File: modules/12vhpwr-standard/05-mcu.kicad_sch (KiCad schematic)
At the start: 7 parts, among them SW1 BOOT, SW2 RESET, U1 ESP32-S3-MINI-1-N4R2

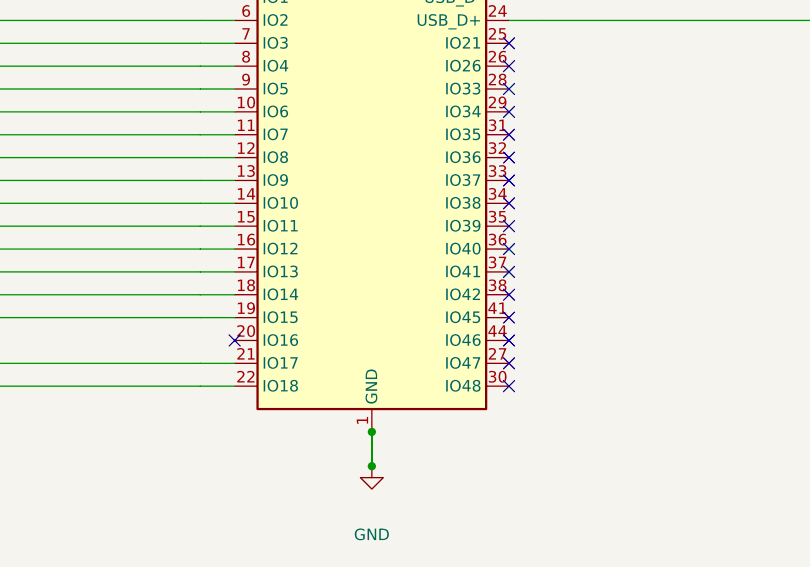
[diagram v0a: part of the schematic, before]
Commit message: All 5 sensing modules: add GPIO0 strapping-pin decoupler (match Hub)
Adds a 0.1uF cap (GPIO0->GND) + 10k pull-up (+3V3->GPIO0) to each module's
MCU sheet, matching the Hub (C8+R11). The modules already had BOOT+RESET
buttons and the EN reset RC; this closes the one systematic gap found in the
2026-07-07 decoupler audit -- the Espressif-recommended strapping-pin RC that
debounces the BOOT button and hardens GPIO0 against spurious download-mode
entry from noise. Owner directive 2026-07-07.

Parts: 24-pin C61/R61, eps/pcie-2/pcie-3 C41/R13, 12vhpwr C25/R24. Each lands
on /GPIO0 = {cap, pull-up, SW1(BOOT), MCU} with cap->GND and pull-up->+3V3,
netlist-verified 0 unexpected changes vs HEAD (an earlier placement that merged
GPIO0 with I2C_SCL/ISENSEP2 was caught by the diff and re-placed in
wire/label-clear space). ERC no_connect_connected=0 on all five.

Co-Authored-By: Claude Opus 4.8 <noreply@anthropic.com>
Claude-Session: https://claude.ai/code/session_01LvfqcnEeuin2oyJQw548EX
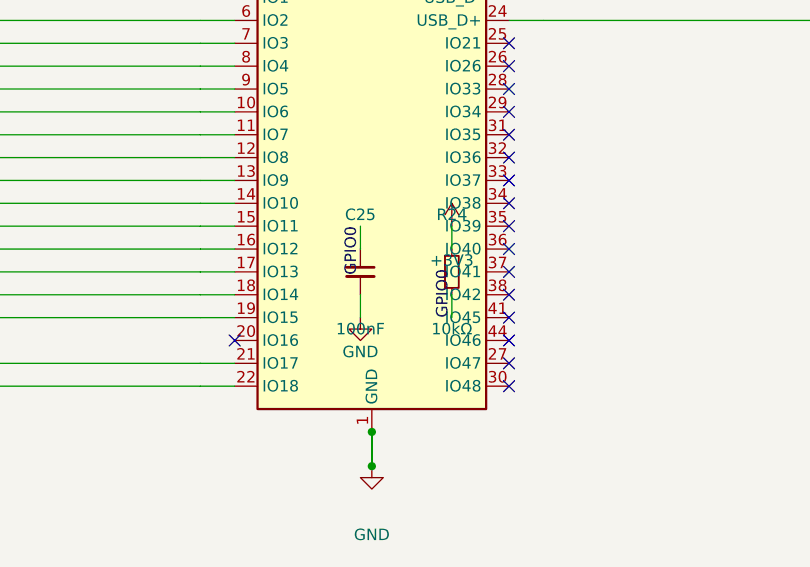
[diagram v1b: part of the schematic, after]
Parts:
- added C25: 100nF, cec-Capacitor_SMD:C_0402_1005Metric, symbol cec-vendor:C_Small
- added R24: 10kΩ, cec-Resistor_SMD:R_0402_1005Metric, symbol cec-vendor:R_Small
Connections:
- net +3V3: now also R24.1
- net GND: now also C25.2
- net GPIO0: now also C25.1, R24.2
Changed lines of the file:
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@@
 	(no_connect (at 257.81 123.19))
 	(no_connect (at 257.81 125.73))
+	(symbol
+		(lib_id "cec-vendor:C_Small")
+		(at 241.3 113.03 0)
+		(unit 1)
+		(exclude_from_sim no)
+		(in_bom yes)
+		(on_board yes)
+		(dnp no)
+		(fields_autoplaced yes)
+		(property "Reference" "C25" (at 241.3 106.68 0) (effects (font (size 1.27 1.27))))
+		(property "Value" "100nF" (at 241.3 119.38 0) (effects (font (size 1.27 1.27))))
+		(property "Footprint" "cec-Capacitor_SMD:C_0402_1005Metric" (at 241.3 113.03 0) (effects (font (size 1.27 1.27)) (hide yes)))
+		(property "Datasheet" "" (at 241.3 113.03 0) (effects (font (size 1.27 1.27)) (hide yes)))
+		(pin "1")
+		(pin "2")
+		(instances
+			(project "12vhpwr-standard-module"
+				(path "/436b24cb-7227-4a56-93c7-4c5d9a5d0058/5e9d5a2e-6b0a-4b6b-9a7a-2f7a7a8a1a05" (reference "C25") (unit 1))
+			)
+		)
+	)
+	(wire (pts (xy 241.3 110.49) (xy 241.3 107.95))
+		(stroke (width 0) (type default)))
+	(label "GPIO0" (at 241.3 107.95 90) (effects (font (size 1.27 1.27)) (justify right bottom)))
+	(wire (pts (xy 241.3 115.57) (xy 241.3 118.11))
+		(stroke (width 0) (type default)))
+	(symbol
+		(lib_id "cec-power:GND")
+		(at 241.3 118.11 0)
+		(unit 1)
+		(exclude_from_sim no)
+		(in_bom yes)
+		(on_board yes)
+		(dnp no)
+		(property "Reference" "#PWR01120" (at 241.3 115.57 0) (effects (font (size 1.27 1.27)) (hide yes)))
+		(property "Value" "GND" (at 241.3 121.92 0) (effects (font (size 1.27 1.27))))
+		(pin "1")
+		(instances
+			(project "12vhpwr-standard-module"
+				(path "/436b24cb-7227-4a56-93c7-4c5d9a5d0058/5e9d5a2e-6b0a-4b6b-9a7a-2f7a7a8a1a05" (reference "#PWR01120") (unit 1))
+			)
+		)
+	)
+	(symbol
+		(lib_id "cec-vendor:R_Small")
+		(at 251.46 113.03 0)
+		(unit 1)
+		(exclude_from_sim no)
+		(in_bom yes)
+		(on_board yes)
+		(dnp no)
+		(fields_autoplaced yes)
+		(property "Reference" "R24" (at 251.46 106.68 0) (effects (font (size 1.27 1.27))))
+		(property "Value" "10kΩ" (at 251.46 119.38 0) (effects (font (size 1.27 1.27))))
+		(property "Footprint" "cec-Resistor_SMD:R_0402_1005Metric" (at 251.46 113.03 0) (effects (font (size 1.27 1.27)) (hide yes)))
+		(property "Datasheet" "" (at 251.46 113.03 0) (effects (font (size 1.27 1.27)) (hide yes)))
+		(pin "1")
+		(pin "2")
+		(instances
+			(project "12vhpwr-standard-module"
+				(path "/436b24cb-7227-4a56-93c7-4c5d9a5d0058/5e9d5a2e-6b0a-4b6b-9a7a-2f7a7a8a1a05" (reference "R24") (unit 1))
+			)
+		)
+	)
+	(wire (pts (xy 251.46 110.49) (xy 251.46 107.95))
+		(stroke (width 0) (type default)))
+	(symbol
+		(lib_id "cec-power:+3V3")
+		(at 251.46 107.95 0)
+		(unit 1)
+		(exclude_from_sim no)
+		(in_bom yes)
+		(on_board yes)
+		(dnp no)
+		(property "Reference" "#PWR01121" (at 251.46 105.41 0) (effects (font (size 1.27 1.27)) (hide yes)))
+		(property "Value" "+3V3" (at 251.46 111.76 0) (effects (font (size 1.27 1.27))))
+		(pin "1")
+		(instances
+			(project "12vhpwr-standard-module"
+				(path "/436b24cb-7227-4a56-93c7-4c5d9a5d0058/5e9d5a2e-6b0a-4b6b-9a7a-2f7a7a8a1a05" (reference "#PWR01121") (unit 1))
+			)
+		)
+	)
+	(wire (pts (xy 251.46 115.57) (xy 251.46 118.11))
+		(stroke (width 0) (type default)))
+	(label "GPIO0" (at 251.46 118.11 270) (effects (font (size 1.27 1.27)) (justify left bottom)))
 	(sheet_instances
 		(path "/5e9d5a2e-6b0a-4b6b-9a7a-2f7a7a8a1a05"

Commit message: 12vhpwr-standard: J2 fan port grows to 3-pin firmware-switched leg
Owner-ratified fan-control leg (3-pin tach, default-on): J2 becomes a
3-pin JST PH B3B-PH-K-S (new cec:CEC_FAN_3P symbol, LCSC C131339, DNP
posture preserved from the prior 2-pin provision). Q1 = AO3400A
low-side NMOS (new reusable cec-vendor:Q_NMOS_GSD symbol) switches the
fan return to GND, default-on via a 10k gate pullup to +3V3 with a
100R series R from a free ESP32-S3 GPIO (IO21); D5 = SS34 flyback
diode across the fan; the open-collector TACH line gets a 10k pullup
plus a 1k series R into a second free GPIO (IO47). Both GPIOs were
picked from the real ERC no_connect list, avoiding the ESP32-S3-MINI-1
N4R2's octal-PSRAM-reserved GPIO26-37 range and the strapping pins.

FAN_EN/FAN_TACH_GPIO are plumbed root-sheet sheet-pin to sheet-pin
into 05-mcu.kicad_sch. ERC is clean (the only growth is the documented
benign lib_symbol_mismatch class, +6 matching every other jellybean
part on this board); the flattened netlist was diffed node-for-node
against the pre-edit baseline and matches exactly: /FAN_12V gains
J2.2+D5.1 and loses only its renumbered old J2 pin, /FAN_RET =
{J2.1,Q1.3,D5.2}, /FAN_TACH = {J2.3,R16.2,R17.2}, /FAN_GATE =
{Q1.1,R14.2,R15.2}, no other net changed.

BOM (bom.csv + jlcpcb.csv) updated; the platform's usual 100R jellybean
(0402WGF1000TCE/C25076) is out of stock at LCSC, so RC0402JR-07100RL
(C106233) was substituted. Datasheets vendored: AO3400A, JST ePH
catalog, Noctua NF-A4x10 FLX (reference fan, consigned -- JST PH is
not the PC-fan KK-2510 standard, so the mating lead/adapter stays an
open item).

Co-Authored-By: Claude Fable 5 <noreply@anthropic.com>
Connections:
- net FAN_EN: now reaches U1.25 (IO21)
- net FAN_TACH_GPIO: now reaches U1.27 (IO47)
- no-connect marks 19 -> 17
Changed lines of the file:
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@@
+		(effects (font (size 1.27 1.27)) (justify left))
+	)
+	(hierarchical_label "FAN_EN"
+		(shape output)
+		(at 283.21 87.63 0)
+		(effects (font (size 1.27 1.27)) (justify left))
+	)
+	(hierarchical_label "FAN_TACH_GPIO"
+		(shape output)
+		(at 283.21 123.19 0)
 		(effects (font (size 1.27 1.27)) (justify left))
 	)
@@
 	(no_connect (at 257.81 74.93))
 	(no_connect (at 257.81 77.47))
-	(no_connect (at 257.81 87.63))
+	(wire (pts (xy 257.81 87.63) (xy 261.62 87.63))
+		(stroke (width 0) (type default)))
+	(wire (pts (xy 261.62 87.63) (xy 283.21 87.63))
+		(stroke (width 0) (type default)))
 	(no_connect (at 257.81 90.17))
 	(no_connect (at 257.81 92.71))
@@
 	(no_connect (at 257.81 118.11))
 	(no_connect (at 257.81 120.65))
-	(no_connect (at 257.81 123.19))
+	(wire (pts (xy 257.81 123.19) (xy 261.62 123.19))
+		(stroke (width 0) (type default)))
+	(wire (pts (xy 261.62 123.19) (xy 283.21 123.19))
+		(stroke (width 0) (type default)))
 	(no_connect (at 257.81 125.73))
 	(symbol
